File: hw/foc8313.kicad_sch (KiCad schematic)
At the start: 62 parts, among them J1 Tag Connect, J2 CAN, J3 CAN, P1 USB_C_Plug, SW1 SW_SPST, U1 DRV8313PWP, U10 XC6206P332MR, U2 STM32F103CBTx, U4 AS5047D, U6 AT24C256C-SSHL-T, U7 LMR36015SFBRNXR, X1 X322516MLB4SI

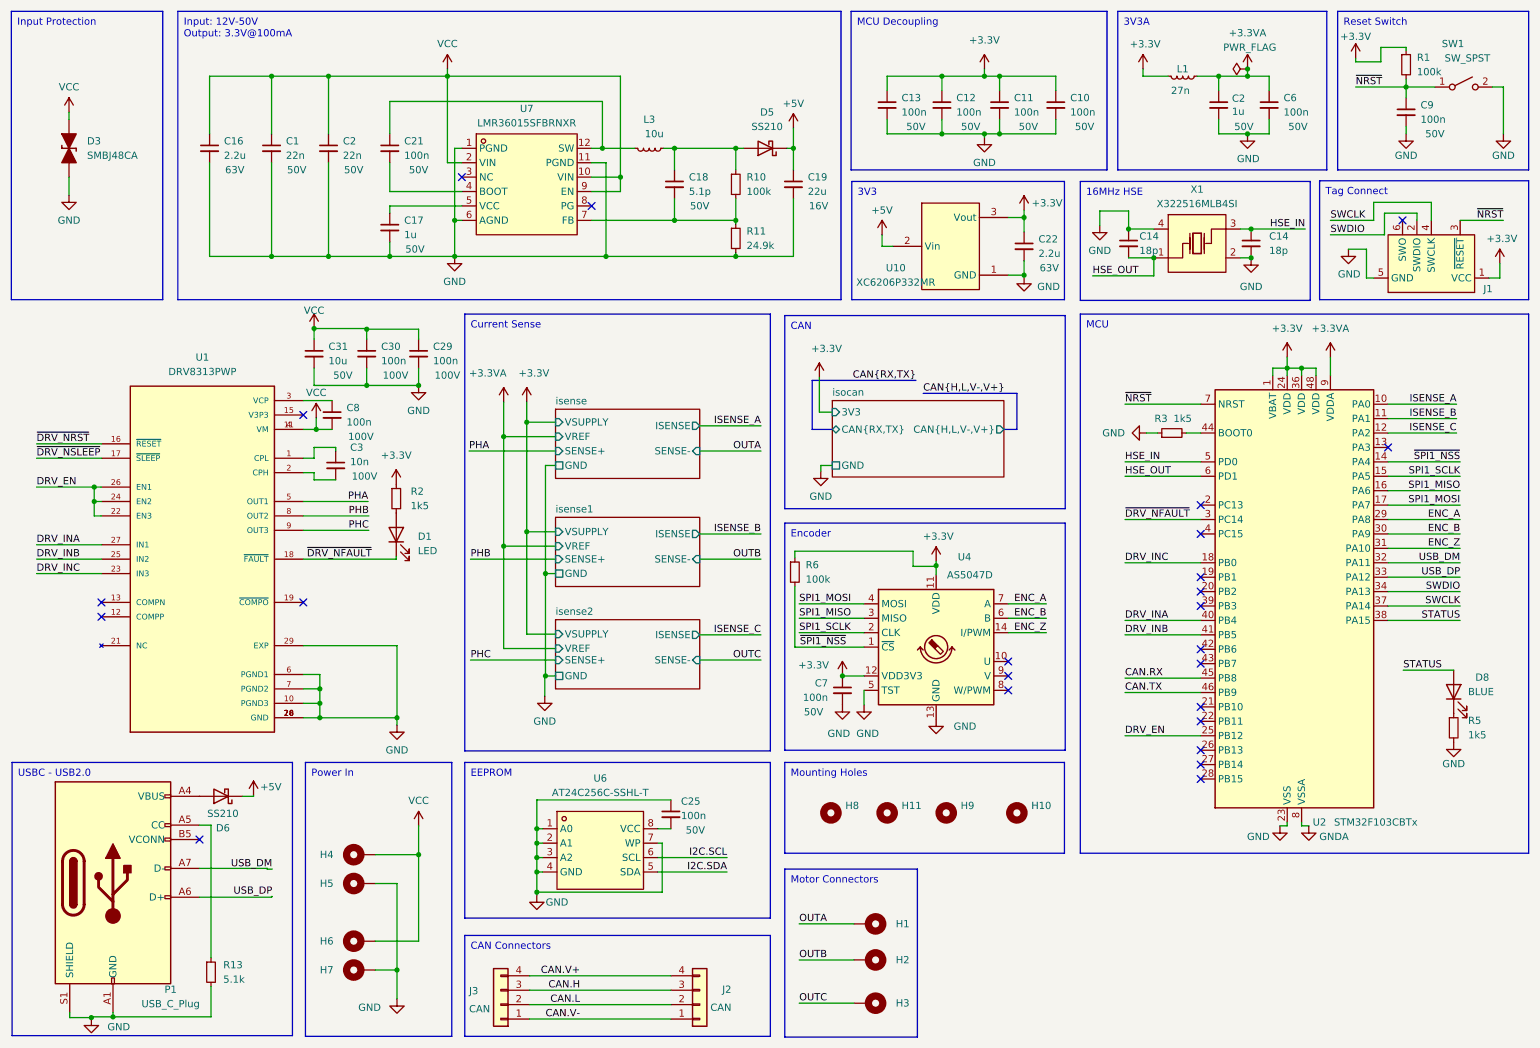
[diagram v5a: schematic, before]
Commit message: [Hw] Squeezing in push button and aux 8 pin connector
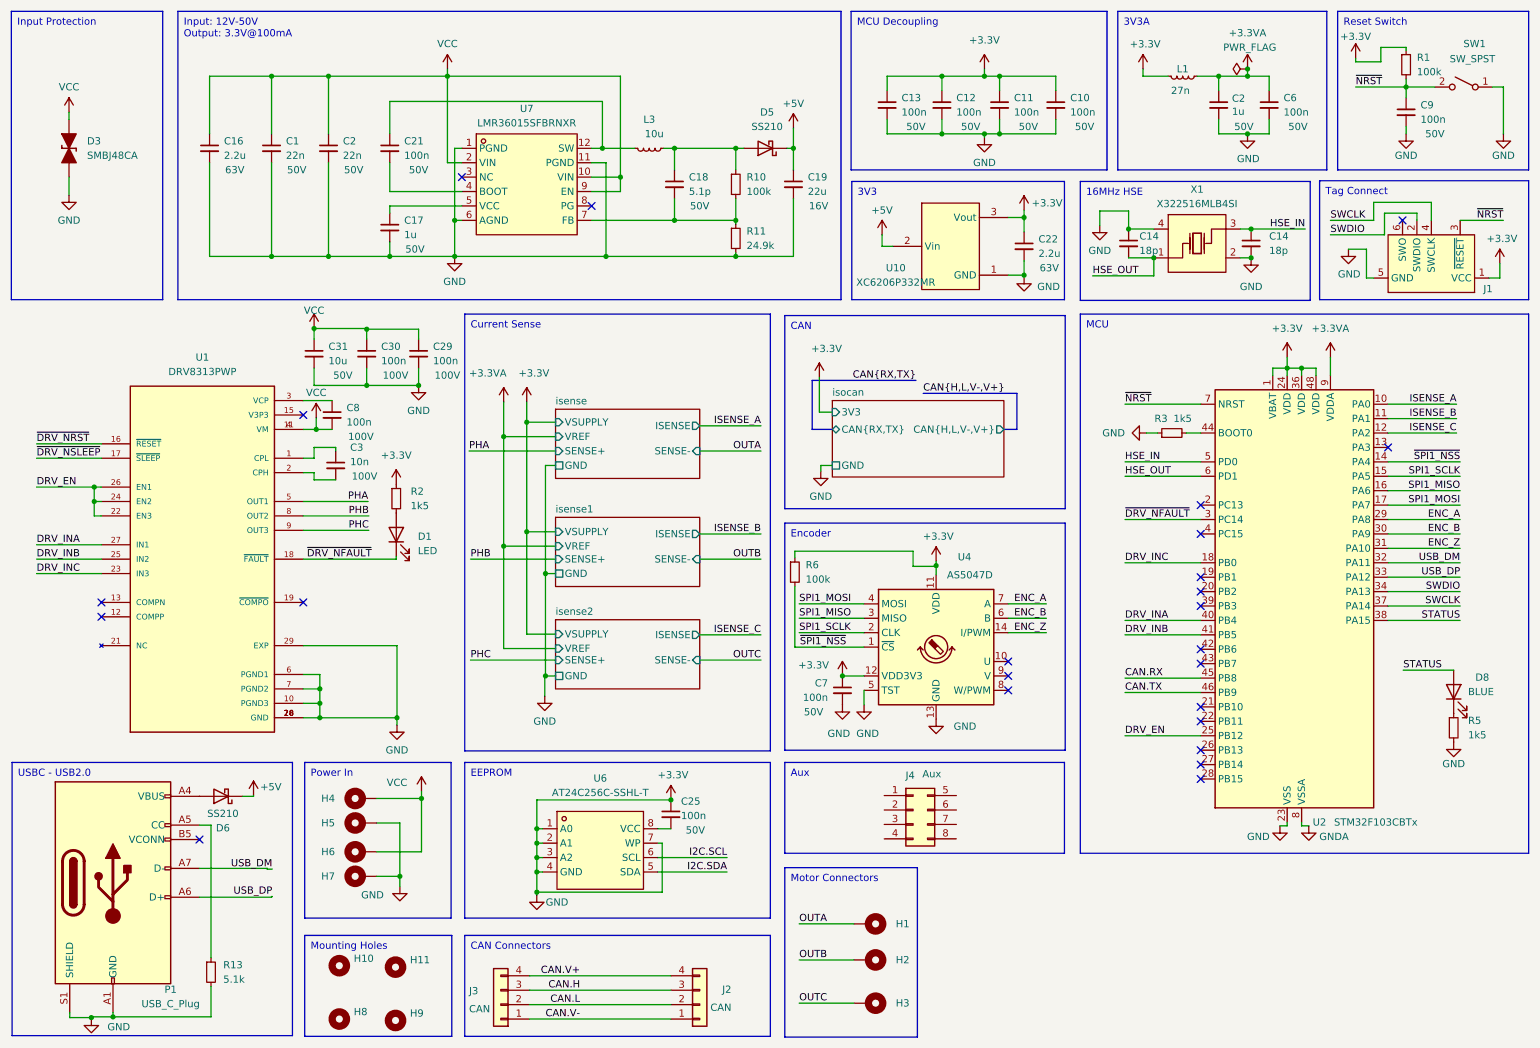
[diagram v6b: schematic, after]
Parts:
- added J4: Aux, Connector_PinHeader_1.00mm:PinHeader_2x04_P1.00mm_Horizontal, symbol Connector_Generic:Conn_02x04_Top_Bottom
- SW1: footprint (none) -> easyeda:SW-SMD_L4.7-W3.5-P3.35-EH
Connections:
- net +3V3: now also C1.2, C10.2, C11.2, C12.2, C13.2, C14.1, C14.2, C16.2, C17.2, C19.2, C2.2, C2.2, C22.2, C25.1, C29.2, C30.2, C31.2, C6.2, C7.2, C9.2, D3.1 (K), H5.1, H7.1, J1.5 (GND), P1.A1 (GND), P1.A12 (GND), P1.B1 (GND), P1.B12 (GND), P1.S1 (SHIELD), R11.2, R13.2, R3.1, R5.2, SW1.1 (A), U1.10 (PGND3), U1.14 (GND), U1.20 (GND), U1.28 (GND), U1.29 (EXP), U1.6 (PGND1), U1.7 (PGND2), U10.1 (GND), U2.23 (VSS), U2.35 (VSS), U2.47 (VSS), U4.13 (GND), U4.5 (TST), U6.1 (A0), U6.2 (A1), U6.3 (A2), U6.4 (GND), U6.7 (WP), U7.1 (PGND), U7.11 (PGND), U7.6 (AGND), X1.2, X1.4
- net ~{NRST}: now also SW1.2 (B); no longer SW1.1 (A)
- removed net GND: C1.2, C10.2, C11.2, C12.2, C13.2, C14.1, C14.2, C16.2, C17.2, C19.2, C2.2, C2.2, C22.2, C25.1, C29.2, C30.2, C31.2, C6.2, C7.2, C9.2, D3.1 (K), H5.1, H7.1, J1.5 (GND), P1.A1 (GND), P1.A12 (GND), P1.B1 (GND), P1.B12 (GND), P1.S1 (SHIELD), R11.2, R13.2, R3.1, R5.2, SW1.2 (B), U1.10 (PGND3), U1.14 (GND), U1.20 (GND), U1.28 (GND), U1.29 (EXP), U1.6 (PGND1), U1.7 (PGND2), U10.1 (GND), U2.23 (VSS), U2.35 (VSS), U2.47 (VSS), U4.13 (GND), U4.5 (TST), U6.1 (A0), U6.2 (A1), U6.3 (A2), U6.4 (GND), U6.7 (WP), U7.1 (PGND), U7.11 (PGND), U7.6 (AGND), X1.2, X1.4
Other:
- moved on the sheet: H10, H11, H4, H5, H6, H7, H8, H9

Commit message: [Hw] Tiny eeprom, all components fit on board!
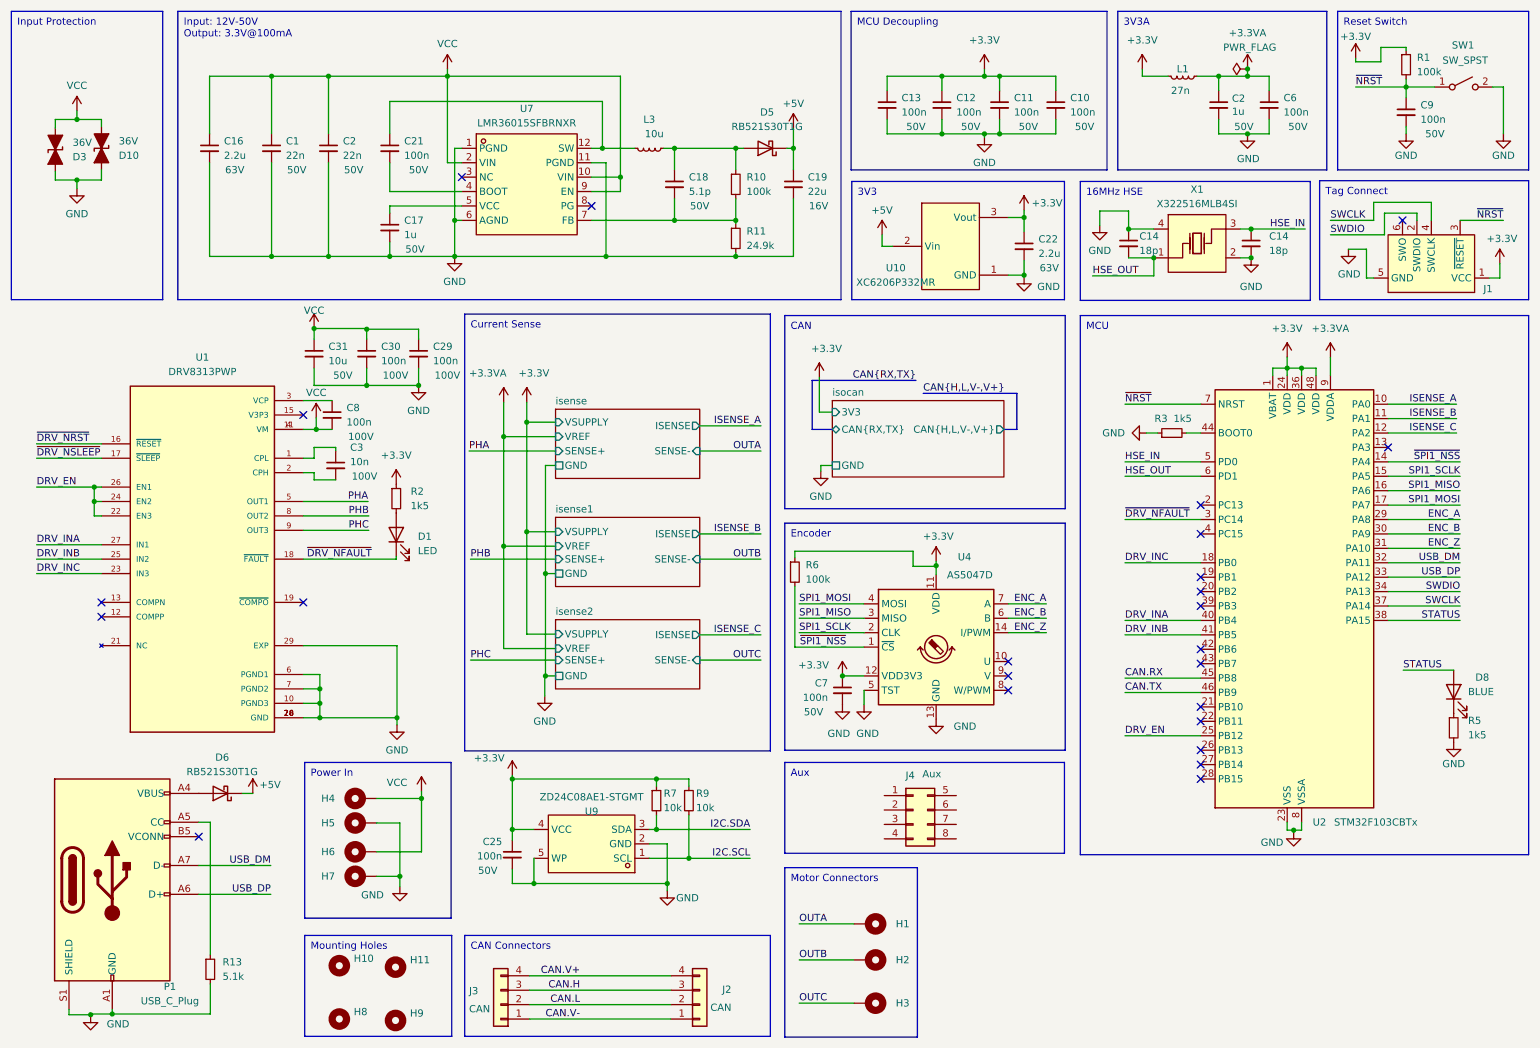
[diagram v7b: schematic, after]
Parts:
- removed D3: SMBJ48CA, Diode_SMD_AKL:D_SMB_TVS, symbol PCM_Diode_TVS_AKL:SMBJ48CA
- removed U6: AT24C256C-SSHL-T, easyeda:SOIC-8_L4.9-W3.9-P1.27-LS6.0-BL, symbol easyeda:AT24C256C-SSHL-T
- added D10, D3: 36V, Diode_SMD:D_SOD-323, symbol Device:D_TVS_Filled
- added R7, R9: 10k, Resistor_SMD:R_0402_1005Metric, symbol Device:R_Small
- added U9: ZD24C08AE1-STGMT, easyeda:SOT-23-5_L3.0-W1.7-P0.95-LS2.8-BL, symbol easyeda:ZD24C08AE1-STGMT
- D1: footprint Diode_SMD:D_0603_1608Metric -> Diode_SMD:D_0402_1005Metric; LCSC C2286 -> C965790
- D5, D6: value SS210 -> RB521S30T1G; footprint Diode_SMD:D_SMA -> Diode_SMD:D_SOD-523; LCSC C14996 -> C145179
- D8: footprint LED_SMD:LED_0603_1608Metric -> LED_SMD:LED_0402_1005Metric; LCSC C19189746 -> C2844007
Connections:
- net GNDA is gone; now on net GND: U2.8 (VSSA)
- net +3.3V: now also C25.1, L1.2, R7.1, R9.1, U9.4 (VCC)
- net +3V3: no longer C1.2, C10.2, C11.2, C12.2, C13.2, C14.1, C14.2, C16.2, C17.2, C19.2, C2.2, C2.2, C22.2, C25.1, C29.2, C30.2, C31.2, C6.2, C7.2, C9.2, H5.1, H7.1, J1.5 (GND), L1.2, P1.A1 (GND), P1.A12 (GND), P1.B1 (GND), P1.B12 (GND), P1.S1 (SHIELD), R11.2, R13.2, R3.1, R5.2, SW1.1 (A), U1.10 (PGND3), U1.14 (GND), U1.20 (GND), U1.28 (GND), U1.29 (EXP), U1.6 (PGND1), U1.7 (PGND2), U10.1 (GND), U2.23 (VSS), U2.35 (VSS), U2.47 (VSS), U4.13 (GND), U4.5 (TST), U7.1 (PGND), U7.11 (PGND), U7.6 (AGND), X1.2, X1.4
- net I2C.SCL: now also R9.2, U9.1 (SCL)
- net I2C.SDA: now also R7.2, U9.3 (SDA)
- net VCC: now also D10.1 (A1), D3.1 (A1)
- net ~{NRST}: now also SW1.1 (A); no longer SW1.2 (B)
- net GND: now reaches C25.2
- net GND: now also C1.2, C10.2, C11.2, C12.2, C13.2, C14.1, C14.2, C16.2, C17.2, C19.2, C2.2, C2.2, C22.2, C29.2, C30.2, C31.2, C6.2, C7.2, C9.2, H5.1, H7.1, J1.5 (GND), P1.A1 (GND), P1.A12 (GND), P1.B1 (GND), P1.B12 (GND), P1.S1 (SHIELD), R11.2, R13.2, R3.1, R5.2, SW1.2 (B), U1.10 (PGND3), U1.14 (GND), U1.20 (GND), U1.28 (GND), U1.29 (EXP), U1.6 (PGND1), U1.7 (PGND2), U10.1 (GND), U2.23 (VSS), U2.35 (VSS), U2.47 (VSS), U4.13 (GND), U4.5 (TST), U7.1 (PGND), U7.11 (PGND), U7.6 (AGND), X1.2, X1.4, D10.2 (A2), D3.2 (A2), U9.2 (GND), U9.5 (WP)
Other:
- moved on the sheet: C25, P1, R13

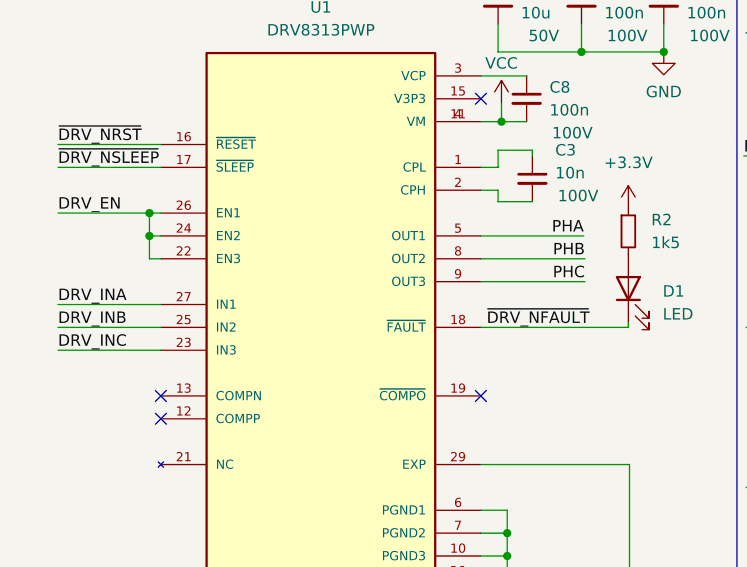
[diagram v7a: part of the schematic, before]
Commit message: [Hw] Simplifying CAN
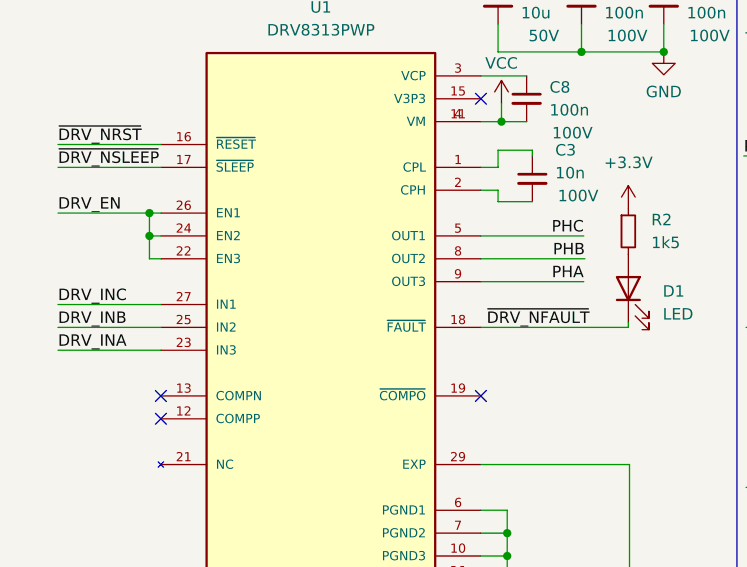
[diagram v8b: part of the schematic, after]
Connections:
- net DRV_INA: now also U1.23 (IN3); no longer U1.27 (IN1)
- net DRV_INC: now also U1.27 (IN1); no longer U1.23 (IN3)
- net PHA: now also U1.9 (OUT3); no longer U1.5 (OUT1)
- net PHC: now also U1.5 (OUT1); no longer U1.9 (OUT3)
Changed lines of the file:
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@@
     (stroke (width 0) (type default))
   )
-  (wire (pts (xy 66.04 106.68) (xy 77.597 106.68))
+  (wire (pts (xy 66.04 106.68) (xy 77.47 106.68))
     (stroke (width 0) (type default))
   )
@@
     (effects (font (size 1.27 1.27)) (justify right bottom))
   )
-  (label "DRV_INA" (at 19.05 109.22 0) (fields_autoplaced)
+  (label "DRV_INA" (at 19.05 114.3 0) (fields_autoplaced)
     (effects (font (size 1.27 1.27)) (justify left bottom))
   )
@@
     (effects (font (size 1.27 1.27)) (justify right bottom))
   )
-  (label "PHC" (at 77.597 106.68 180) (fields_autoplaced)
+  (label "PHC" (at 77.47 101.6 180) (fields_autoplaced)
     (effects (font (size 1.27 1.27)) (justify right bottom))
   )
@@
     (effects (font (size 1.27 1.27)) (justify right bottom))
   )
-  (label "DRV_INC" (at 19.05 114.3 0) (fields_autoplaced)
+  (label "DRV_INC" (at 19.05 109.22 0) (fields_autoplaced)
     (effects (font (size 1.27 1.27)) (justify left bottom))
   )
@@
     (effects (font (size 1.27 1.27)) (justify right bottom))
   )
-  (label "PHA" (at 77.47 101.6 180) (fields_autoplaced)
-    (effects (font (size 1.27 1.27)) (justify right bottom))
-  )
+  (label "PHA" (at 77.47 106.68 180) (fields_autoplaced)
+    (effects (font (size 1.27 1.27)) (justify right bottom))
+  )
